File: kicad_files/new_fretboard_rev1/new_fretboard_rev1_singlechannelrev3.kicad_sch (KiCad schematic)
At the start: 22 parts, among them U2 LX3302AQPW-TR-EASY

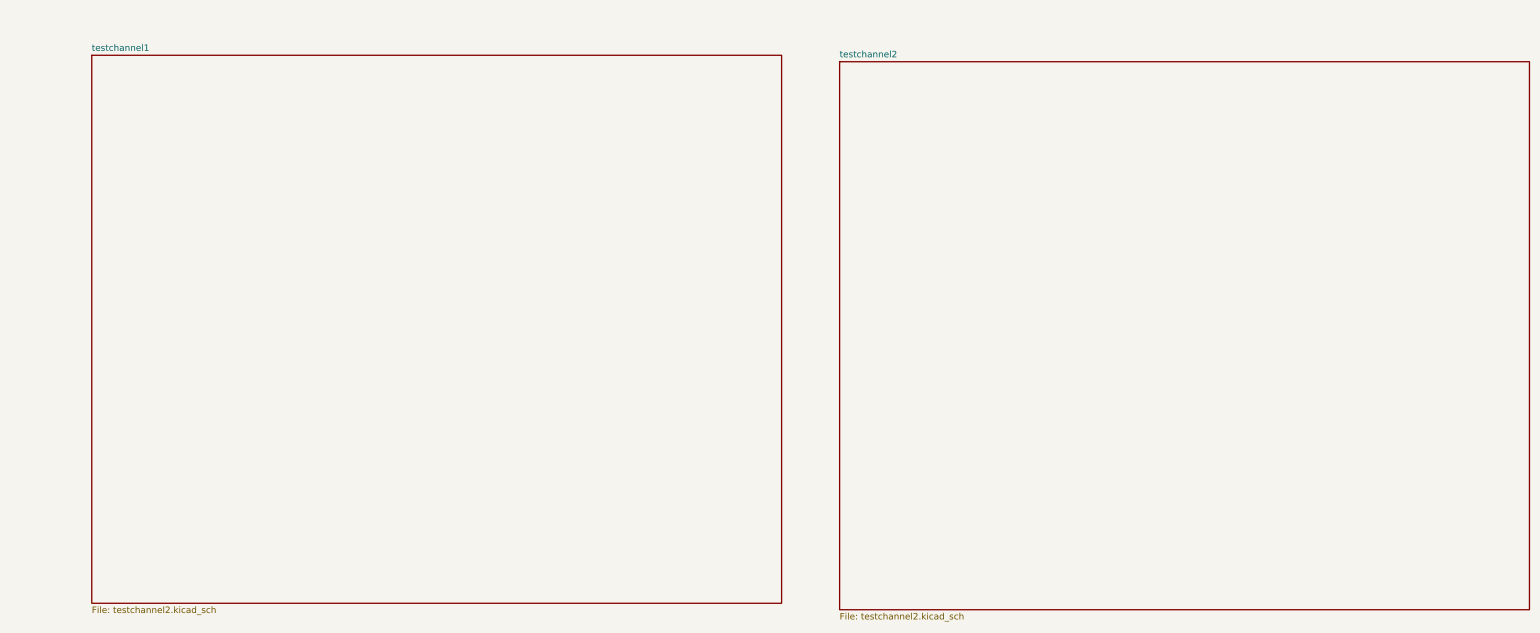
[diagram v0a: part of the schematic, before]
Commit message: version with three coil circuits, some errors
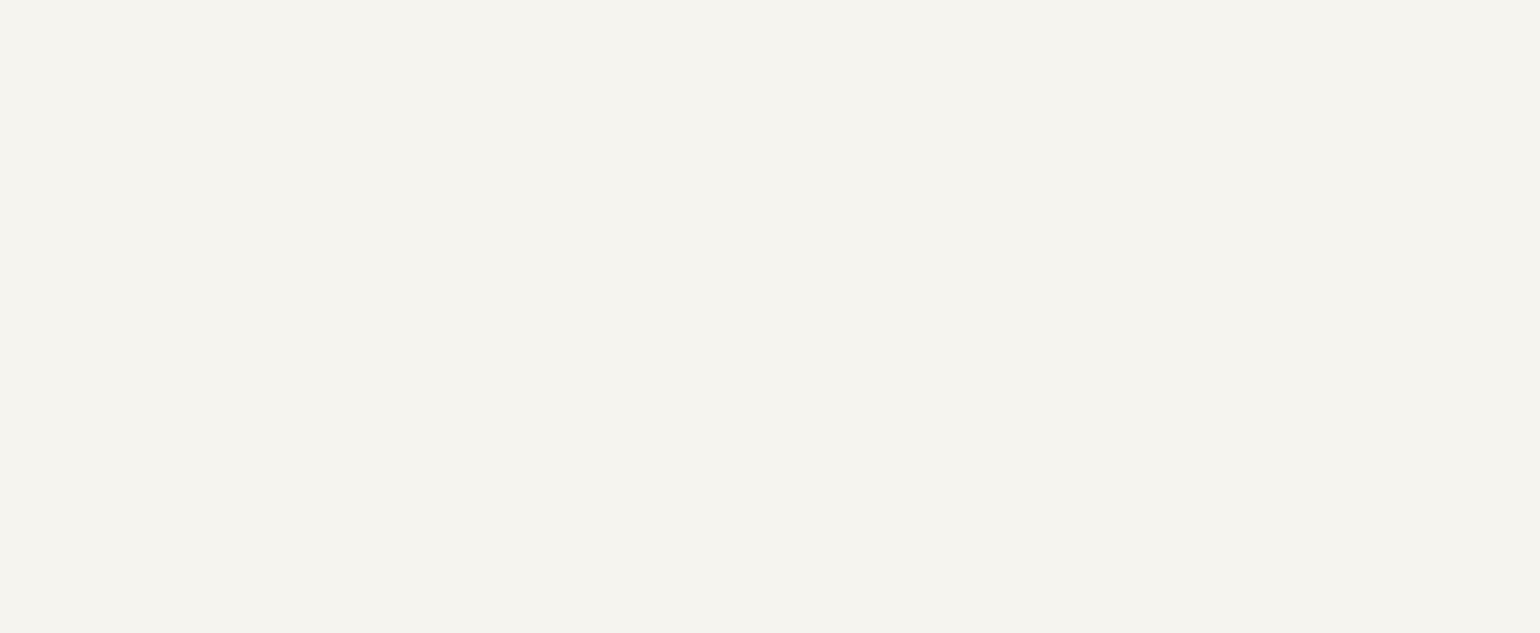
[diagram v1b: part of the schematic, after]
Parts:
- C12, C13, C14, C15, C16, C17, C18, C19, C20, C21, C22, L5, L6, L7, L8, R10, R11, R12, R13, R8, R9, U2: Component Class ch1 -> (none)
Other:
- removed sheet testchannel1
- removed sheet testchannel2
